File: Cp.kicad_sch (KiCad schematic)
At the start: 64 parts, among them Q10 J201, Q11 J201, Q3 2SC1815, Q4 2SC1815, Q5 2SC1815, Q6 2SC1815, Q7 2SC1815, Q8 2SC1815, Q9 2SC1815, SW1 SW_Push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

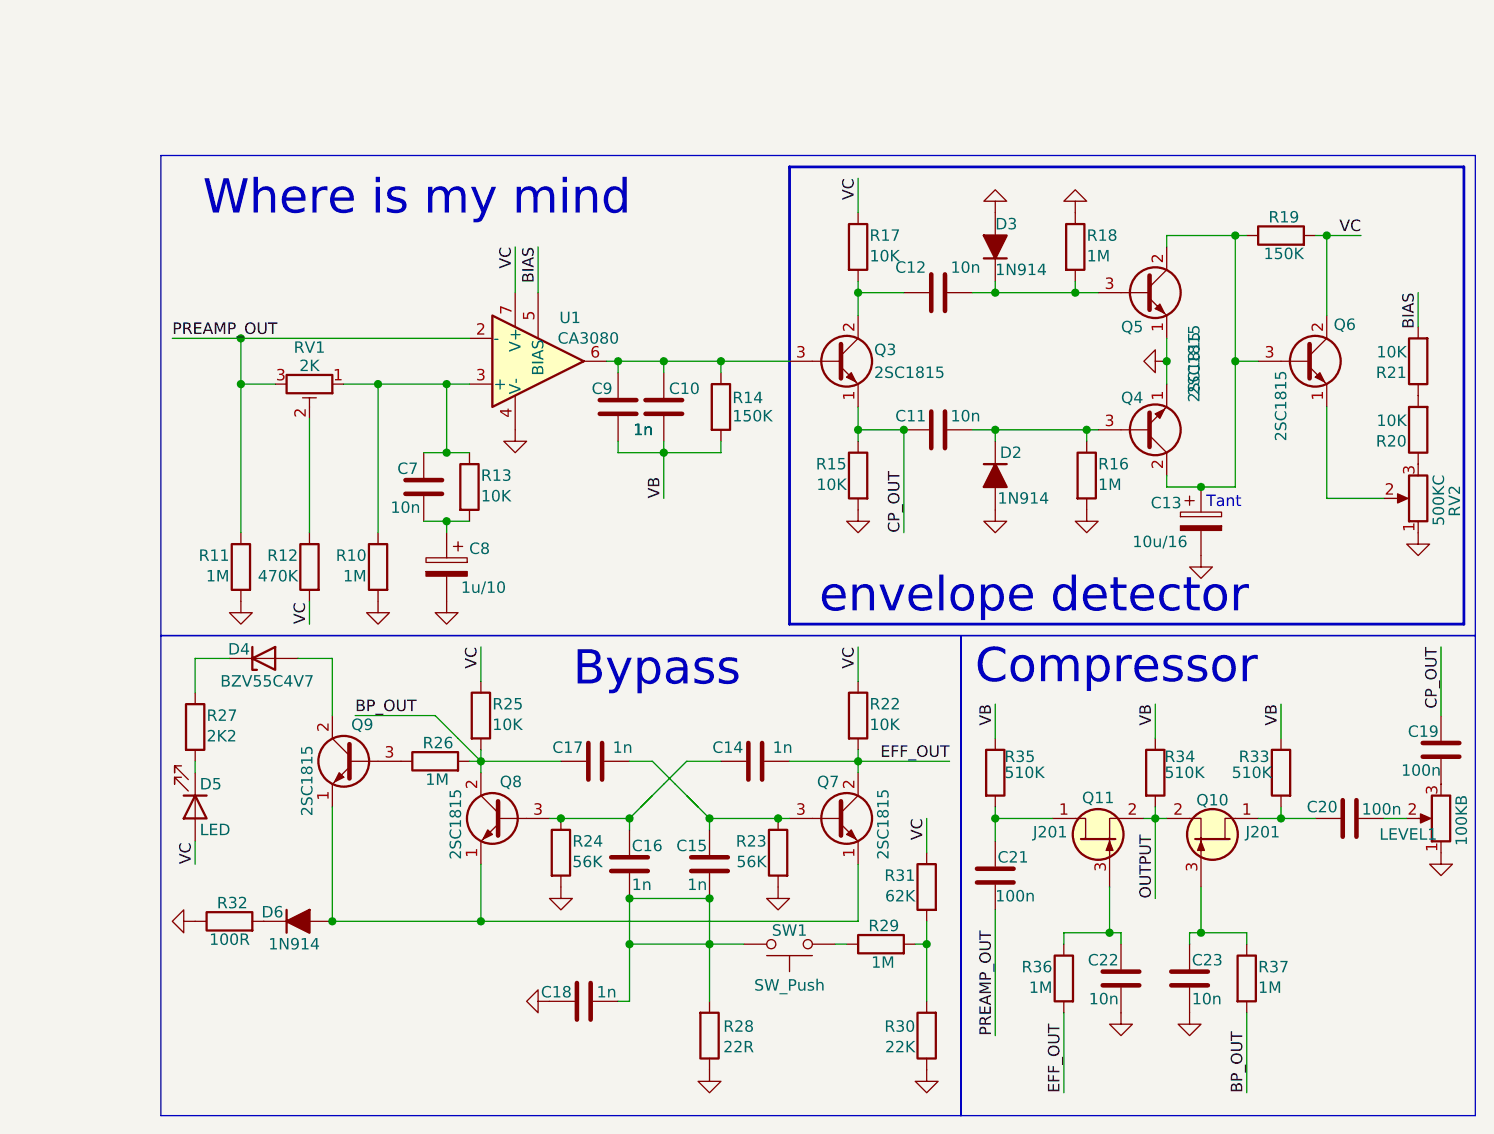
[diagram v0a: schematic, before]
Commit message: Schem upd
added Voltage supply
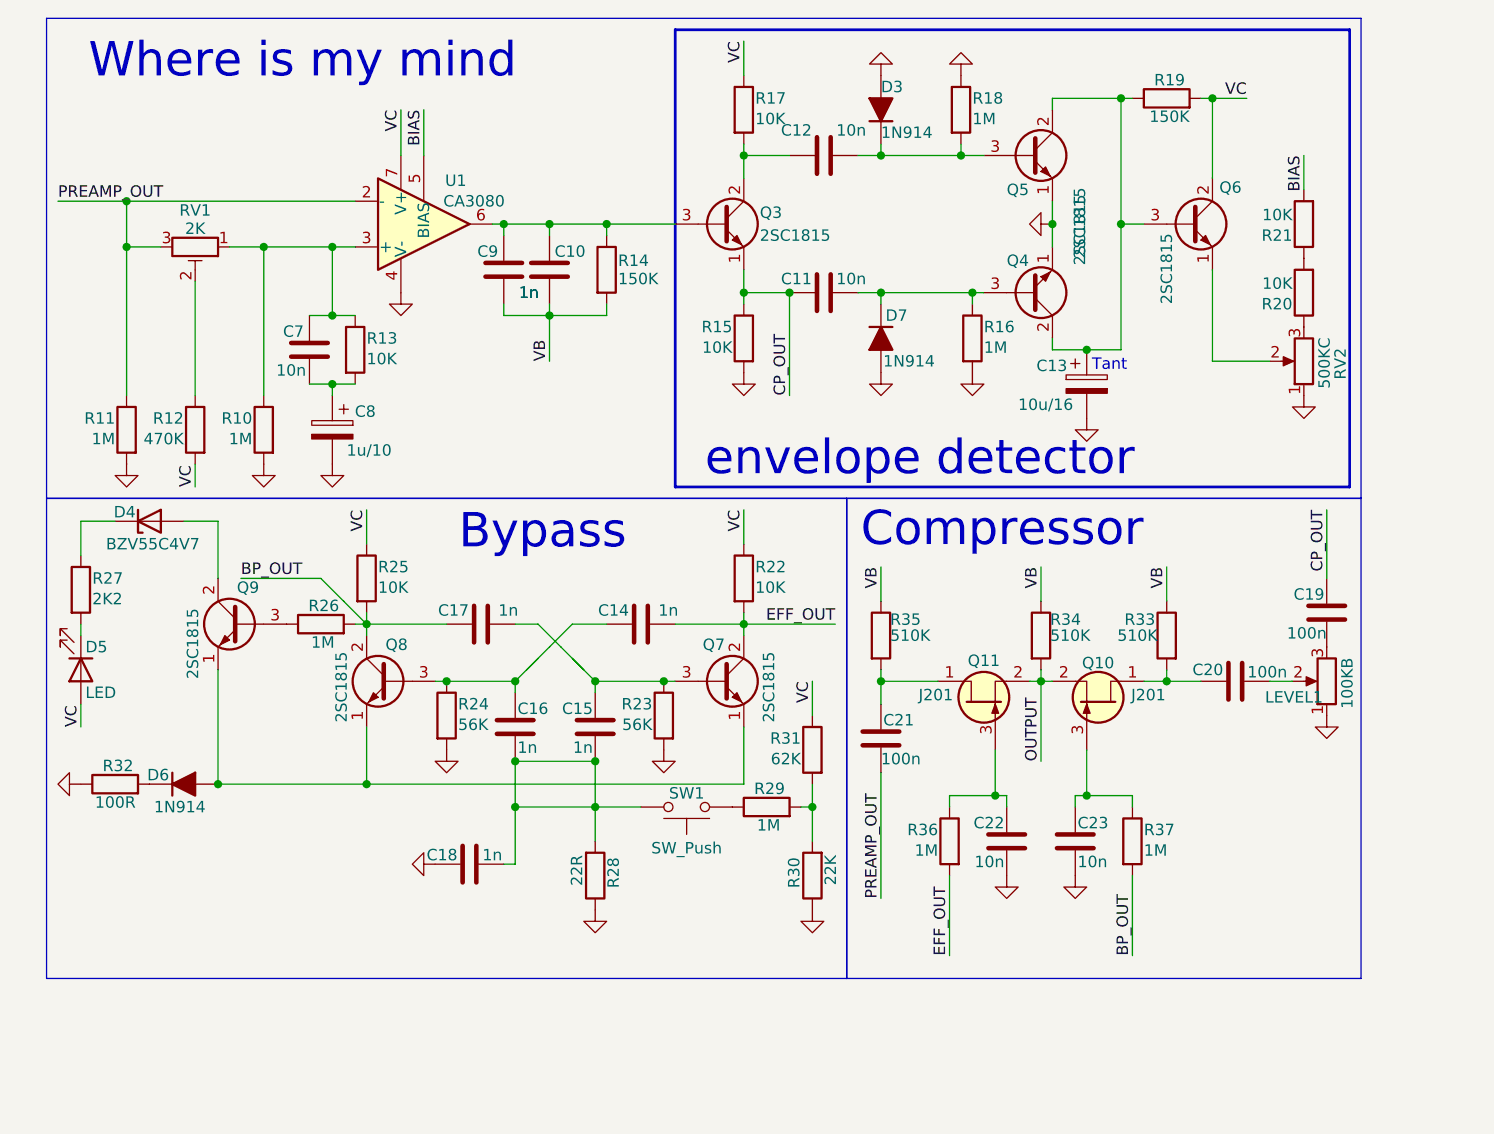
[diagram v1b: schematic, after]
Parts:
- removed D2: 1N914, PCM_Diode_THT_AKL:D_DO-35_SOD27_P7.62mm_Horizontal, symbol PCM_Diode_AKL:1N914
- added D7: 1N914, PCM_Diode_THT_AKL:D_DO-35_SOD27_P7.62mm_Horizontal, symbol PCM_Diode_AKL:1N914
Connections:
- net GND: now also D7.2 (A)
- net at C11.2, Q4.3 (B), R16.1: now also D7.1 (K)
